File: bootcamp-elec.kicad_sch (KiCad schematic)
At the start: 0 parts

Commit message: create schema & adapt sym
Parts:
- added C1, C2: 12pF, symbol bootcamp-elec:Capacitor
- added C3, C4, C7: 100nF, symbol bootcamp-elec:Capacitor
- added C6: 1uF, symbol bootcamp-elec:Capacitor
- added D1: Red, symbol bootcamp-elec:Diode
- added D2: Green, symbol bootcamp-elec:Diode
- added J1, J2: ~, symbol bootcamp-elec:Conn_12
- added J3: FTDI, symbol bootcamp-elec:FTDI
- added R1, R3: 10K, symbol bootcamp-elec:Resistor
- added R2: 330, symbol bootcamp-elec:Resistor
- added SW1: SW_Push, symbol bootcamp-elec:SW_Push
- added U1: ATmega328P-A, symbol bootcamp-elec:ATmega328P-A
- added Y1: 16MHz, symbol bootcamp-elec:Crystal
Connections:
- new net: D1.2, R1.1
- new net: C2.1, U1.7 (XTAL1/PB6), Y1.1
- new net: C3.2, U1.20 (AREF)
- new net: C1.2, U1.8 (XTAL2/PB7), Y1.3
- new net: D2.1, R2.1
- new net: C4.1, SW1.1
- new net A0: J2.8, U1.23 (PC0)
- new net A1: J2.7, U1.24 (PC1)
- new net A2: J2.6, U1.25 (PC2)
- new net A3: J2.5, U1.26 (PC3)
- new net A4: U1.27 (PC4)
- new net A5: U1.28 (PC5)
- new net A6: U1.19 (ADC6)
- new net A7: U1.22 (ADC7)
- new net D10: J2.12, U1.14 (PB2)
- new net D2: J1.8, U1.32 (PD2)
- new net D3: J1.7, U1.1 (PD3)
- new net D4: J1.6, U1.2 (PD4)
- new net D5: J1.5, U1.9 (PD5)
- new net D6: J1.4, U1.10 (PD6)
- new net D7: J1.3, U1.11 (PD7)
- new net D8: J1.2, U1.12 (PB0)
- new net D9: J1.1, U1.13 (PB1)
- new net DTR: J1.10, J2.3, J3.1, R3.1, SW1.2, U1.29 (RESET/PC6)
- new net GND: C1.1, C2.2, C4.2, C6.1, C7.2, D2.2, J1.9, J2.2, J3.5, J3.6, R1.2, U1.21 (GND), U1.3 (GND), U1.5 (GND), Y1.2, Y1.4
- new net MISO: J2.10, U1.16 (PB4)
- new net MOSI: J2.11, U1.15 (PB3)
- new net RXI: J1.11, J3.3, U1.30 (PD0)
- new net SCK: J2.9, R2.2, U1.17 (PB5)
- new net TXO: J1.12, J3.2, U1.31 (PD1)
- new net VCC: C3.1, C6.2, C7.1, D1.1, J2.1, J2.4, J3.4, R3.2, U1.18 (AVCC), U1.4 (VCC), U1.6 (VCC)
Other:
- note added: "Activity"
- note added: "Power"
- note added: "Reset"
- company: (none) -> 42Chips
- title: (none) -> Bootcamp-elec

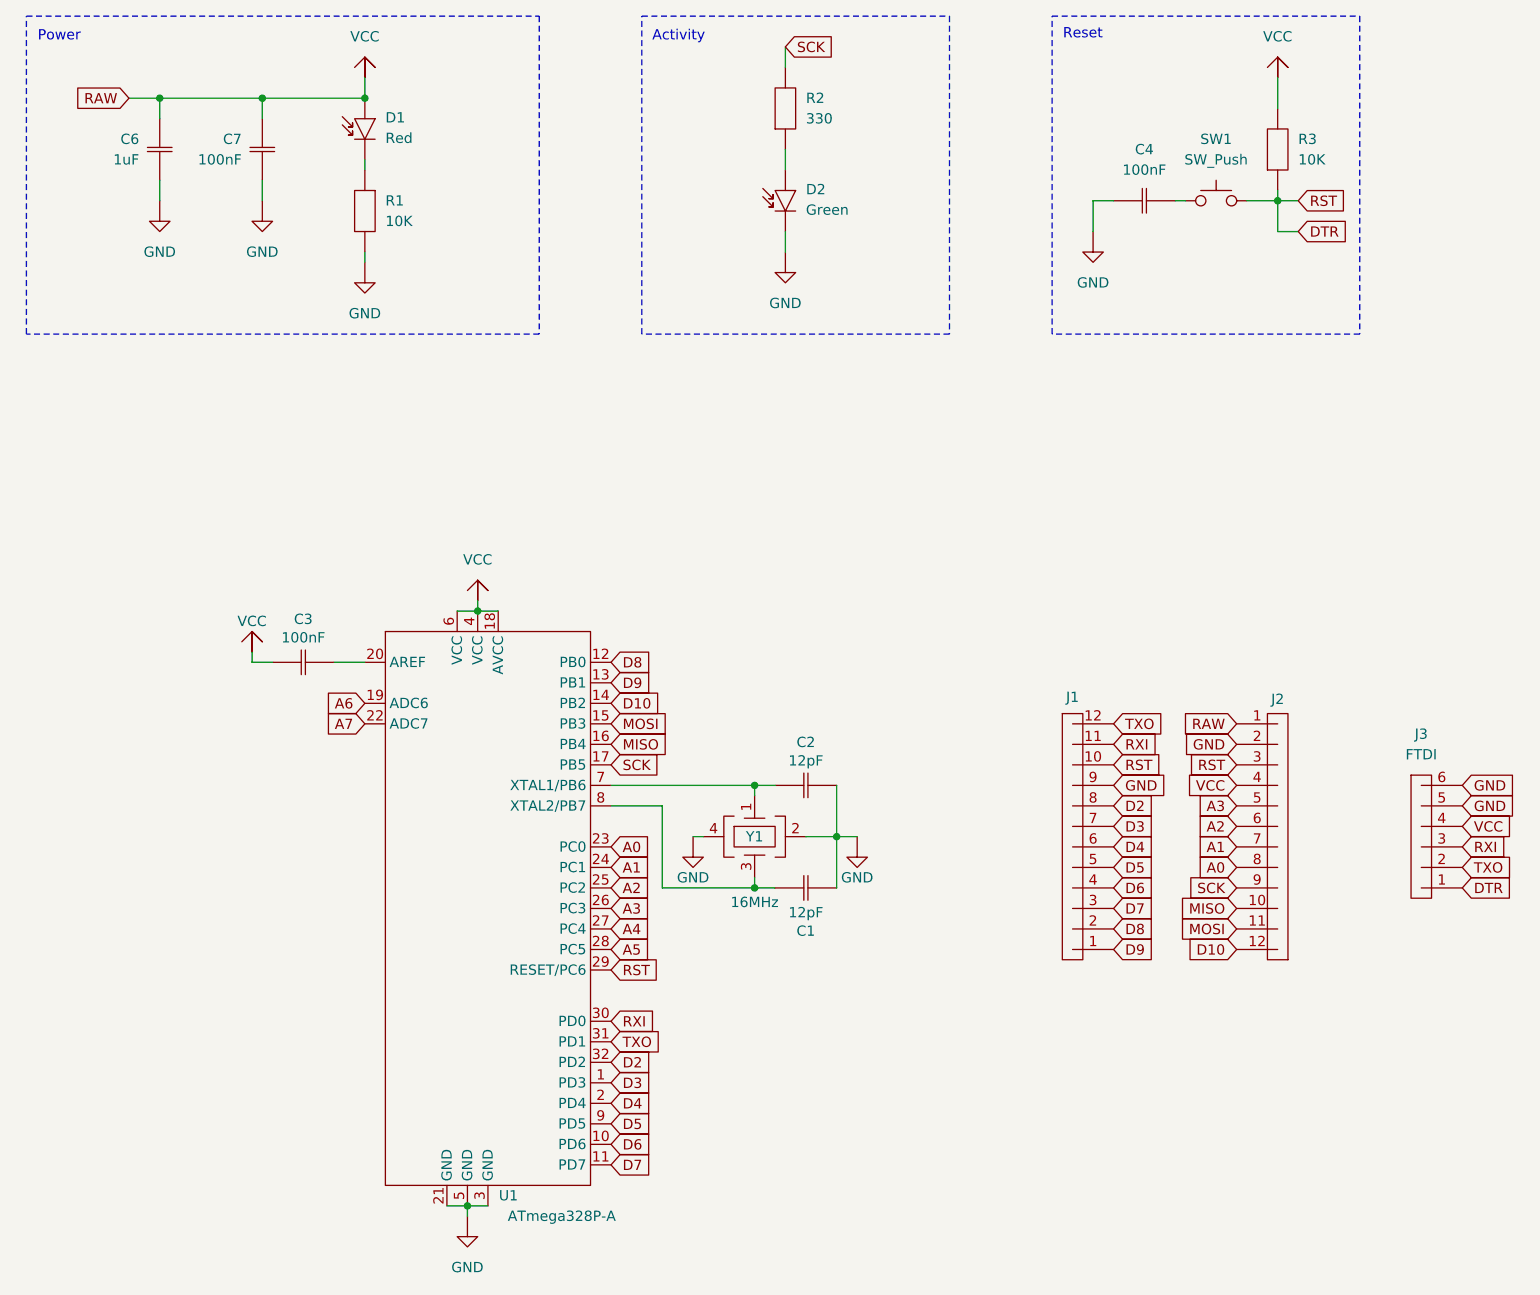
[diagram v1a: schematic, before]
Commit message: ERC no errors
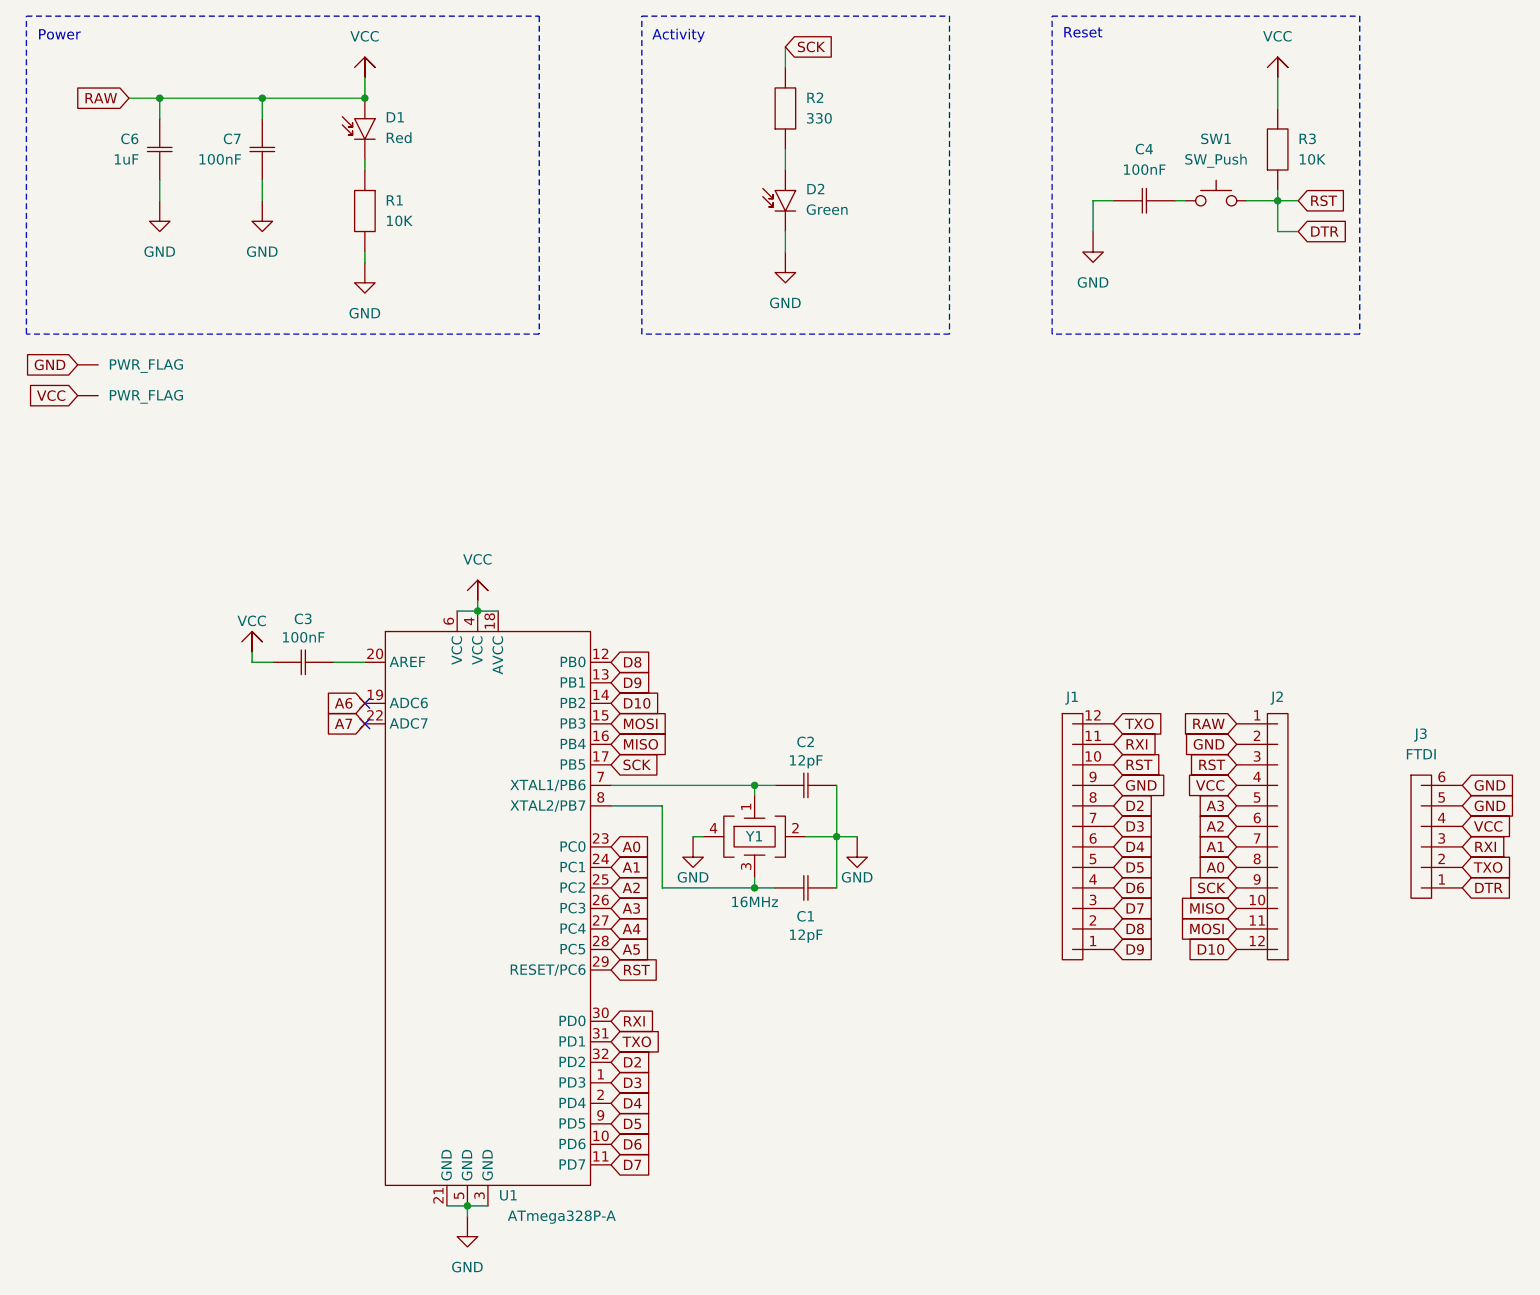
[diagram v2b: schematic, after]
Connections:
- net GND: now also C1.2; no longer C1.1
- net at U1.8 (XTAL2/PB7), Y1.3: now also C1.1; no longer C1.2
- no-connect marks 0 -> 2
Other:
- moved on the sheet: C1
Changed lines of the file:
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@@
 		(color 0 0 0 0)
 	)
+	(no_connect
+		(at 60.96 106.68)
+	)
+	(no_connect
+		(at 60.96 104.14)
+	)
 	(wire
 		(pts
@@
 		)
 	)
+	(global_label "GND"
+		(shape input)
+		(at 25.4 62.23 180)
+		(fields_autoplaced yes)
+		(effects
+			(font
+				(size 1.27 1.27)
+			)
+			(justify right)
+		)
+		(property "Intersheetrefs" "${INTERSHEET_REFS}"
+			(at 18.5443 62.23 0)
+			(effects
+				(font
+					(size 1.27 1.27)
+				)
+				(justify right)
+				(hide yes)
+			)
+		)
+	)
 	(global_label "SCK"
 		(shape input)
@@
 		)
 	)
+	(global_label "VCC"
+		(shape input)
+		(at 25.4 66.04 180)
+		(fields_autoplaced yes)
+		(effects
+			(font
+				(size 1.27 1.27)
+			)
+			(justify right)
+		)
+		(property "Intersheetrefs" "${INTERSHEET_REFS}"
+			(at 18.7862 66.04 0)
+			(effects
+				(font
+					(size 1.27 1.27)
+				)
+				(justify right)
+				(hide yes)
+			)
+		)
+	)
 	(global_label "RAW"
 		(shape input)
@@
 		(dnp no)
 		(fields_autoplaced yes)
-		(property "Reference" "#VCC02"
+		(property "Reference" "#VCC2"
 			(at 60.96 28.194 0)
 			(effects
@@
 			(project "bootcamp-elec"
 				(path "/51290277-cbe4-4803-9089-ca803c735dcd"
-					(reference "#VCC02")
+					(reference "#VCC2")
 					(unit 1)
 				)
@@
 		(dnp no)
 		(fields_autoplaced yes)
-		(property "Reference" "#GND03"
+		(property "Reference" "#GND3"
 			(at 48.26 40.386 0)
 			(effects
@@
 			(project "bootcamp-elec"
 				(path "/51290277-cbe4-4803-9089-ca803c735dcd"
-					(reference "#GND03")
+					(reference "#GND3")
 					(unit 1)
 				)
@@
 		(dnp no)
 		(fields_autoplaced yes)
-		(property "Reference" "#VCC03"
+		(property "Reference" "#VCC3"
 			(at 173.99 28.194 0)
 			(effects
@@
 			(project "bootcamp-elec"
 				(path "/51290277-cbe4-4803-9089-ca803c735dcd"
-					(reference "#VCC03")
+					(reference "#VCC3")
 					(unit 1)
 				)
@@
 		(dnp no)
 		(fields_autoplaced yes)
-		(property "Reference" "#GND05"
+		(property "Reference" "#GND5"
 			(at 113.03 46.736 0)
 			(effects
@@
 			(project "bootcamp-elec"
 				(path "/51290277-cbe4-4803-9089-ca803c735dcd"
-					(reference "#GND05")
+					(reference "#GND5")
 					(unit 1)
 				)
@@
 	)
 	(symbol
+		(lib_id "bootcamp-elec:PWR_FLAG")
+		(at 25.4 62.23 90)
+		(unit 1)
+		(exclude_from_sim no)
+		(in_bom yes)
+		(on_board yes)
+		(dnp no)
+		(fields_autoplaced yes)
+		(property "Reference" "#PWR_FLAG1"
+			(at 29.718 62.23 0)
+			(effects
+				(font
+					(size 1.27 1.27)
+				)
+				(hide yes)
+			)
+		)
+		(property "Value" "PWR_FLAG"
+			(at 29.21 62.2299 90)
+			(effects
+				(font
+					(size 1.27 1.27)
+				)
+				(justify right)
+			)
+		)
+		(property "Footprint" ""
+			(at 25.4 62.23 0)
+			(effects
+				(font
+					(size 1.27 1.27)
+				)
+				(hide yes)
+			)
+		)
+		(property "Datasheet" ""
+			(at 25.4 62.23 0)
+			(effects
+				(font
+					(size 1.27 1.27)
+				)
+				(hide yes)
+			)
+		)
+		(property "Description" ""
+			(at 25.4 62.23 0)
+			(effects
+				(font
+					(size 1.27 1.27)
+				)
+				(hide yes)
+			)
+		)
+		(pin "1"
+		)
+		(instances
+			(project "bootcamp-elec"
+				(path "/51290277-cbe4-4803-9089-ca803c735dcd"
+					(reference "#PWR_FLAG1")
+					(unit 1)
+				)
+			)
+		)
+	)
+	(symbol
 		(lib_id "bootcamp-elec:GND")
 		(at 121.92 120.65 180)
@@
 	(symbol
 		(lib_id "bootcamp-elec:Capacitor")
-		(at 115.57 127 180)
+		(at 115.57 127 0)
 		(unit 1)
 		(exclude_from_sim no)
@@
 		(dnp no)
 		(property "Reference" "C1"
-			(at 115.57 132.334 0)
+			(at 115.57 130.556 0)
 			(effects
 				(font
@@
 		)
 		(property "Value" "12pF"
-			(at 115.57 130.048 0)
+			(at 115.57 132.842 0)
 			(effects
 				(font
@@
 		(dnp no)
 		(fields_autoplaced yes)
-		(property "Reference" "#GND06"
+		(property "Reference" "#GND6"
 			(at 151.13 44.196 0)
 			(effects
@@
 			(project "bootcamp-elec"
 				(path "/51290277-cbe4-4803-9089-ca803c735dcd"
-					(reference "#GND06")
+					(reference "#GND6")
+					(unit 1)
+				)
+			)
+		)
+	)
+	(symbol
+		(lib_id "bootcamp-elec:PWR_FLAG")
+		(at 25.4 66.04 90)
+		(unit 1)
+		(exclude_from_sim no)
+		(in_bom yes)
+		(on_board yes)
+		(dnp no)
+		(fields_autoplaced yes)
+		(property "Reference" "#PWR_FLAG2"
+			(at 29.718 66.04 0)
+			(effects
+				(font
+					(size 1.27 1.27)
+				)
+				(hide yes)
+			)
+		)
+		(property "Value" "PWR_FLAG"
+			(at 29.21 66.0399 90)
+			(effects
+				(font
+					(size 1.27 1.27)
+				)
+				(justify right)
+			)
+		)
+		(property "Footprint" ""
+			(at 25.4 66.04 0)
+			(effects
+				(font
+					(size 1.27 1.27)
+				)
+				(hide yes)
+			)
+		)
+		(property "Datasheet" ""
+			(at 25.4 66.04 0)
+			(effects
+				(font
+					(size 1.27 1.27)
+				)
+				(hide yes)
+			)
+		)
+		(property "Description" ""
+			(at 25.4 66.04 0)
+			(effects
+				(font
+					(size 1.27 1.27)
+				)
+				(hide yes)
+			)
+		)
+		(pin "1"
+		)
+		(instances
+			(project "bootcamp-elec"
+				(path "/51290277-cbe4-4803-9089-ca803c735dcd"
+					(reference "#PWR_FLAG2")
 					(unit 1)
 				)
@@
 		(dnp no)
 		(fields_autoplaced yes)
-		(property "Reference" "#GND02"
+		(property "Reference" "#GND2"
 			(at 35.56 40.386 0)
 			(effects
@@
 			(project "bootcamp-elec"
 				(path "/51290277-cbe4-4803-9089-ca803c735dcd"
-					(reference "#GND02")
+					(reference "#GND2")
 					(unit 1)
 				)
@@
 		(dnp no)
 		(fields_autoplaced yes)
-		(property "Reference" "#GND04"
+		(property "Reference" "#GND4"
 			(at 60.96 48.006 0)
 			(effects
@@
 			(project "bootcamp-elec"
 				(path "/51290277-cbe4-4803-9089-ca803c735dcd"
-					(reference "#GND04")
+					(reference "#GND4")
 					(unit 1)
 				)
@@
 		(dnp no)
 		(property "Reference" "J2"
-			(at 173.99 103.632 0)
+			(at 173.99 103.378 0)
 			(effects
 				(font

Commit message: fix refs
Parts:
- renumbered D2 to D1, D1 to D2, R2 to R1, R1 to R2

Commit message: create footprint lib
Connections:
- net GND: now also D1.1; no longer D1.2
- net VCC: now also D2.2; no longer D2.1
- net at R2.1: now also D2.1; no longer D2.2
- net at R1.1: now also D1.2; no longer D1.1

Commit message: add silkscreen logo & pcb config
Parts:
- C1, C2, C3, C4, C6, C7: footprint (none) -> bootcamp-elec:C_0805_2012Metric
- D1, D2: footprint (none) -> bootcamp-elec:LED_0805_2012Metric
- J1, J2: footprint (none) -> bootcamp-elec:PinHeader_1x12_P2.54mm_Vertical
- J3: footprint (none) -> bootcamp-elec:PinHeader_1x06_P2.54mm_Vertical
- R1, R2, R3: footprint (none) -> bootcamp-elec:R_0805_2012Metric
- SW1: footprint (none) -> bootcamp-elec:SW_Tact_6X6mm_H5mm_SMD
- U1: footprint (none) -> bootcamp-elec:TQFP-32_7x7mm_P0.8mm
- Y1: footprint (none) -> bootcamp-elec:Crystal_SMD_3225-4Pin_3.2x2.5mm
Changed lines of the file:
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@@
 			)
 		)
-		(property "Footprint" ""
+		(property "Footprint" "bootcamp-elec:R_0805_2012Metric"
 			(at 60.96 43.18 0)
 			(effects
@@
 			)
 		)
-		(property "Footprint" ""
+		(property "Footprint" "bootcamp-elec:C_0805_2012Metric"
 			(at 115.57 114.3 0)
 			(effects
@@
 			)
 		)
-		(property "Footprint" ""
+		(property "Footprint" "bootcamp-elec:TQFP-32_7x7mm_P0.8mm"
 			(at 76.2 120.65 0)
 			(effects
@@
 			)
 		)
-		(property "Footprint" ""
+		(property "Footprint" "bootcamp-elec:LED_0805_2012Metric"
 			(at 113.03 41.91 0)
 			(effects
@@
 			)
 		)
-		(property "Footprint" ""
+		(property "Footprint" "bootcamp-elec:C_0805_2012Metric"
 			(at 35.56 35.56 0)
 			(effects
@@
 			)
 		)
-		(property "Footprint" ""
+		(property "Footprint" "bootcamp-elec:C_0805_2012Metric"
 			(at 157.48 41.91 0)
 			(effects
@@
 			)
 		)
-		(property "Footprint" ""
+		(property "Footprint" "bootcamp-elec:C_0805_2012Metric"
 			(at 48.26 35.56 0)
 			(effects
@@
 			)
 		)
-		(property "Footprint" ""
+		(property "Footprint" "bootcamp-elec:R_0805_2012Metric"
 			(at 113.03 30.48 0)
 			(effects
@@
 			)
 		)
-		(property "Footprint" ""
+		(property "Footprint" "bootcamp-elec:C_0805_2012Metric"
 			(at 115.57 127 0)
 			(effects
@@
 			)
 		)
-		(property "Footprint" ""
+		(property "Footprint" "bootcamp-elec:C_0805_2012Metric"
 			(at 53.34 99.06 0)
 			(effects
@@
 			)
 		)
-		(property "Footprint" ""
+		(property "Footprint" "bootcamp-elec:LED_0805_2012Metric"
 			(at 60.96 33.02 0)
 			(effects
@@
 			)
 		)
-		(property "Footprint" ""
+		(property "Footprint" "bootcamp-elec:SW_Tact_6X6mm_H5mm_SMD"
 			(at 166.37 41.91 0)
 			(effects
@@
 			)
 		)
-		(property "Footprint" ""
+		(property "Footprint" "bootcamp-elec:R_0805_2012Metric"
 			(at 173.99 35.56 0)
 			(effects
@@
 			)
 		)
-		(property "Footprint" ""
+		(property "Footprint" "bootcamp-elec:Crystal_SMD_3225-4Pin_3.2x2.5mm"
 			(at 109.22 120.65 0)
 			(effects
@@
 			)
 		)
-		(property "Footprint" ""
+		(property "Footprint" "bootcamp-elec:PinHeader_1x12_P2.54mm_Vertical"
 			(at 148.59 120.65 0)
 			(effects
@@
 			)
 		)
-		(property "Footprint" ""
+		(property "Footprint" "bootcamp-elec:PinHeader_1x06_P2.54mm_Vertical"
 			(at 191.77 120.65 0)
 			(effects
@@
 			)
 		)
-		(property "Footprint" ""
+		(property "Footprint" "bootcamp-elec:PinHeader_1x12_P2.54mm_Vertical"
 			(at 173.99 120.65 0)
 			(effects
